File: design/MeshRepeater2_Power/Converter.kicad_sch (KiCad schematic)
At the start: 43 parts, among them U2 TPS63802DLAR

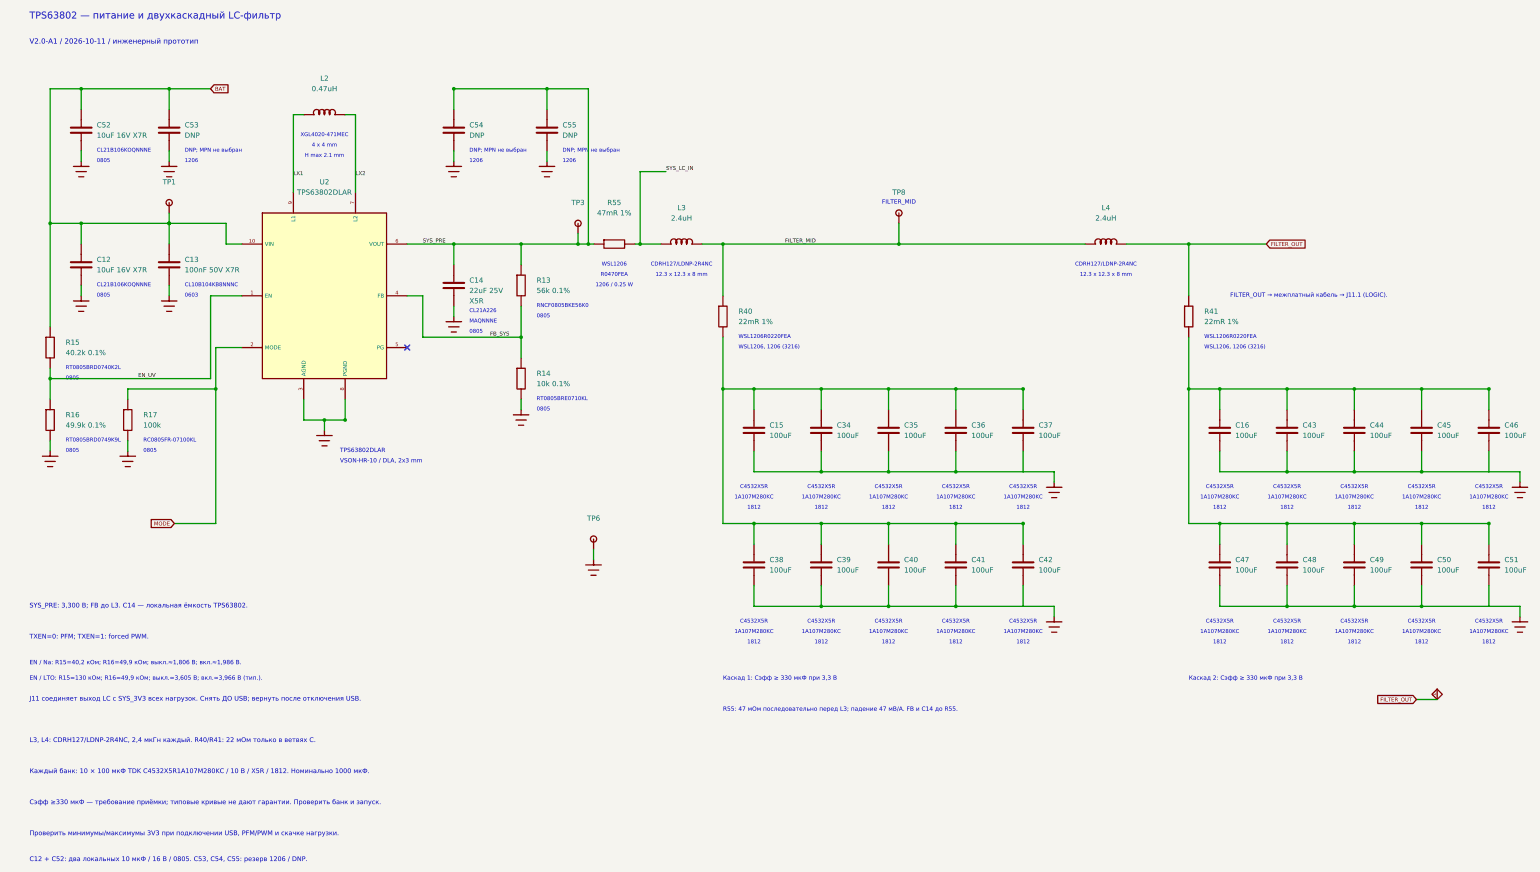
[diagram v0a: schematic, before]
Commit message: Publish Mesh Repeater 2.0 A2
Add INA219 battery measurement with a 0.1 ohm shunt and vertical
12-pin interconnects through the middle shield. Publish updated
POWER, LOGIC and SHIELD KiCad sources, local models, BOM and A2
documentation with the completed routing and ground-via audit.

Preserve the V1 baseline and archives inside the V2 branch.
Validation: independent review 132/132; final artifact gate 499/499.
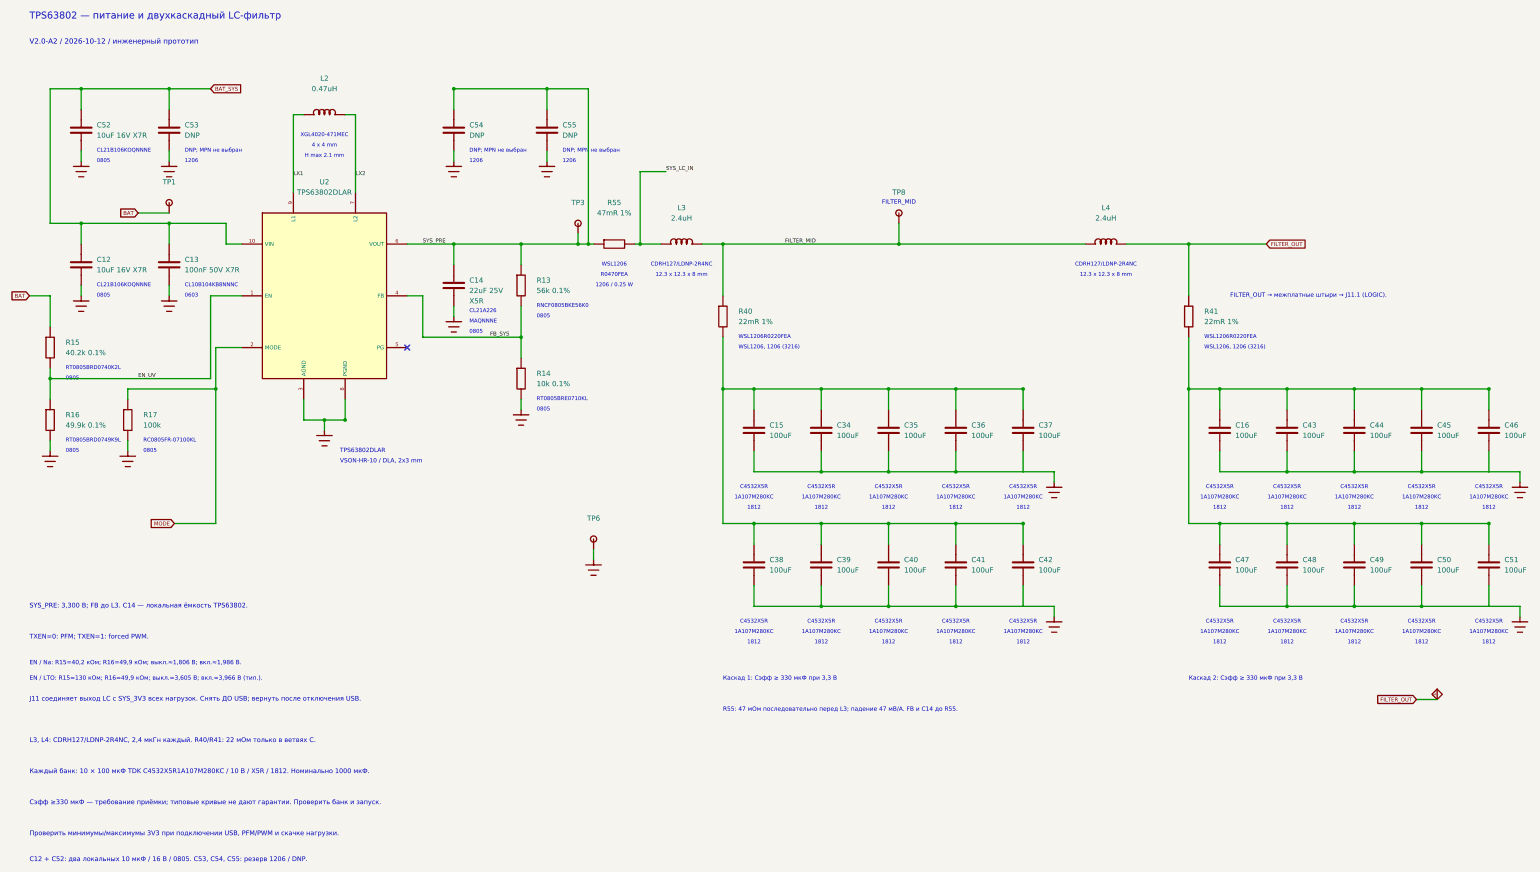
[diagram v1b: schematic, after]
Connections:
- net BAT: no longer C12.1, C13.1, C52.1, C53.1, U2.10 (VIN)
- new net BAT_SYS: C12.1, C13.1, C52.1, C53.1, U2.10 (VIN)
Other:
- note added: "FILTER_OUT → межплатные штыри → J11.1 (LOGIC)."
- note added: "V2.0-A2 / 2026-10-12 / инженерный прототип"
- note removed: "FILTER_OUT → межплатный кабель → J11.1 (LOGIC)."
- note removed: "V2.0-A1 / 2026-10-11 / инженерный прототип"
